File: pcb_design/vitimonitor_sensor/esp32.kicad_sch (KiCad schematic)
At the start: 5 parts, among them U2 ESP32-C3-WROOM-02U

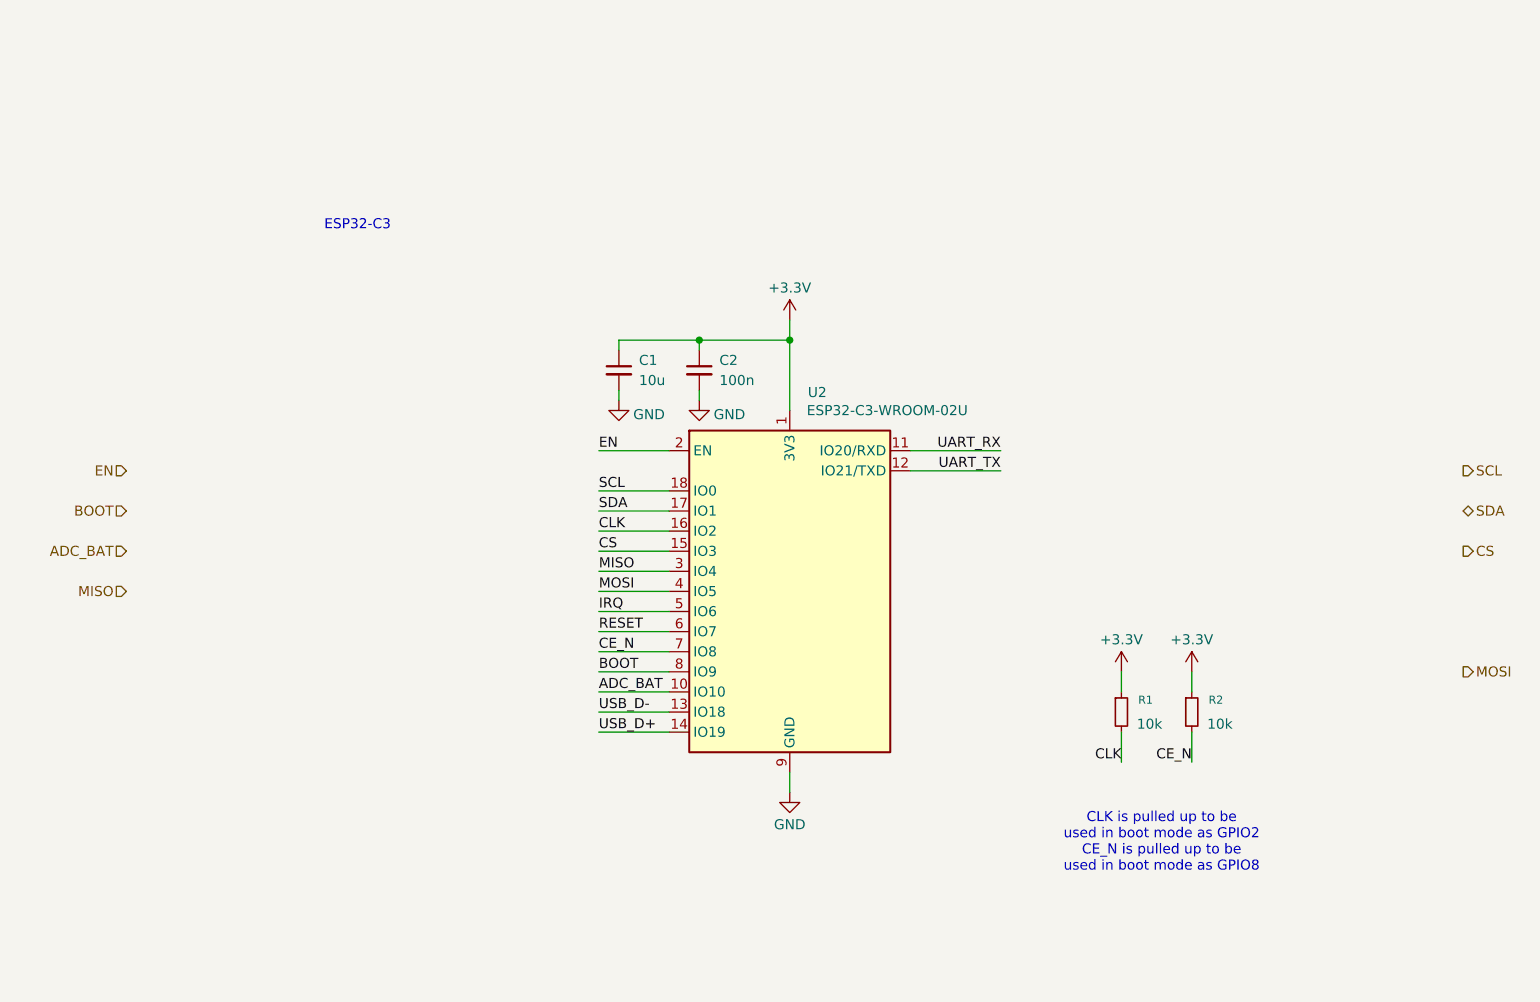
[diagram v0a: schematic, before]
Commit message: Schematic update, hierarchical approach done, missing SX1261
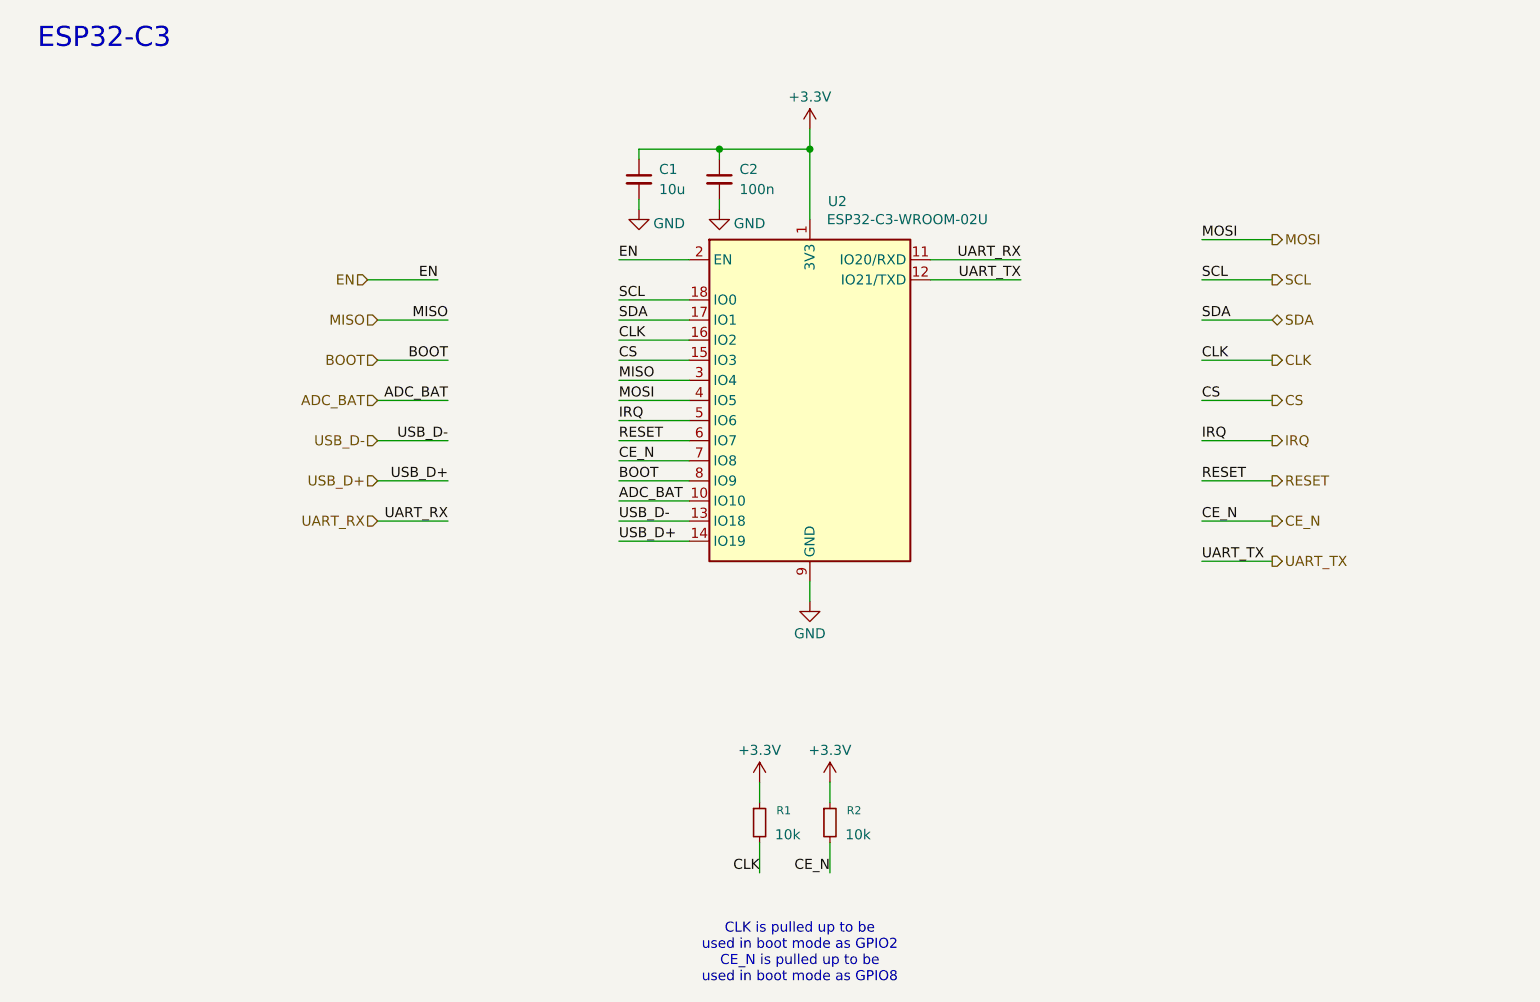
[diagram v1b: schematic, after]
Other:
- moved on the sheet: C1, C2, R1, R2, U2
